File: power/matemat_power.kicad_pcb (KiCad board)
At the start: 2 copper layers, 220 x 77 mm, 153 parts, among them IC1 74HC4094, IC2 74HC4094, IC3 ULN2803A, IC4 PC817, J1 B3_Wago, J101 Output, J11 CONN_8, J2 B3_Wago, J201 Output, J3 B3_Wago, J301 Output, J4 MAIN_BOARD_BUS, J401 Output, J501 Output, J6 B3_Wago, J601 Output, J7 B3_Wago, J701 Output, J801 Output, Q1 NPN_BCE, Q4 ZXMP7A17G, T101 BT136, T201 BT136, T301 BT136, T401 BT136, T501 BT136, T601 BT136, T701 BT136, T801 BT136, U101 MOC3022M, U201 MOC3022M, U301 MOC3022M, U401 MOC3022M, U501 MOC3022M, U6 TPS40200D, U601 MOC3022M, U701 MOC3022M, U801 MOC3022M

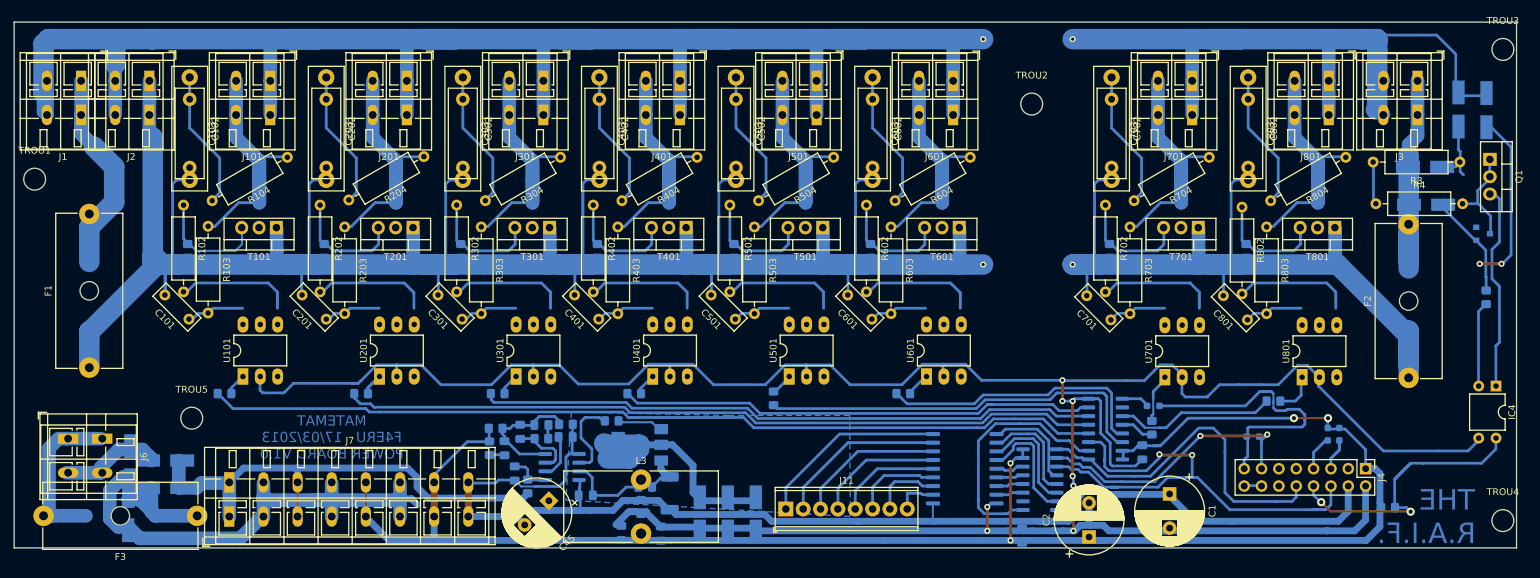
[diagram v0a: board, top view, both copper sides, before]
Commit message: Replaced power board diode pad layouts
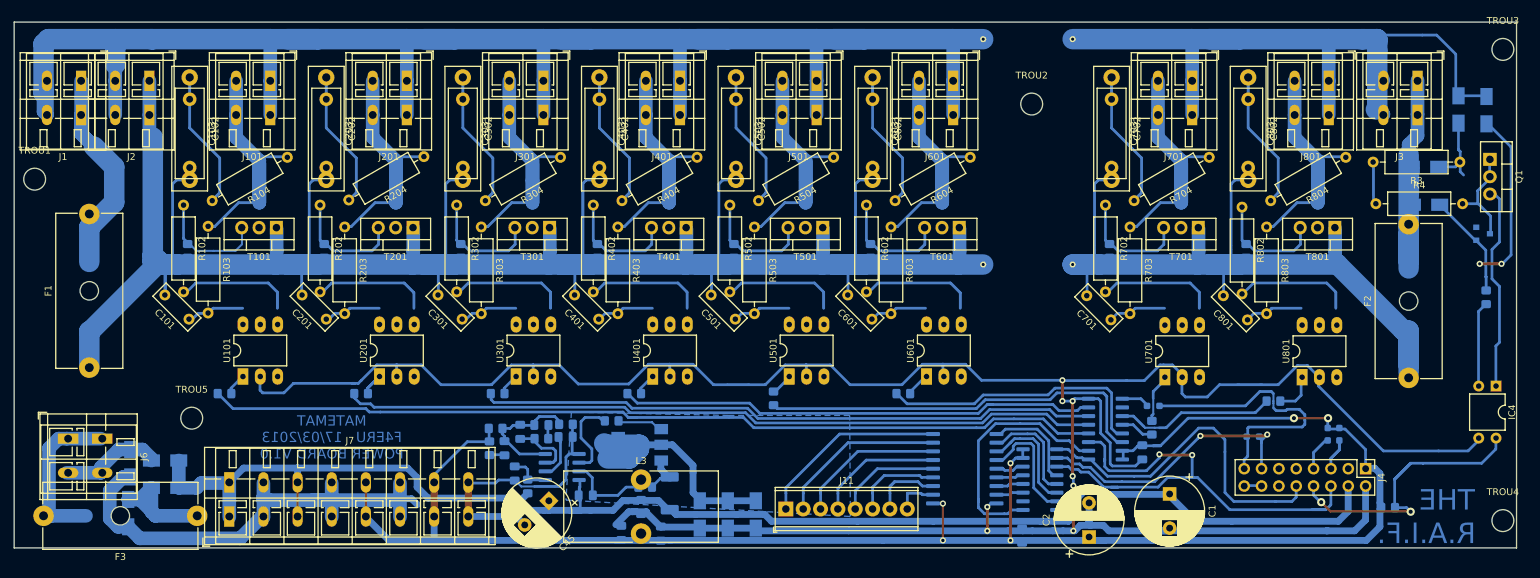
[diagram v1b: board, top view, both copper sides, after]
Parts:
- D1, D10, D11, D2, D3, D4, D5, D6, D7, D8, D9: footprint Diode_SMD:D_SMA_Handsoldering -> Diode_SMD:D_SMA
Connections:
- net Net-(D5-Pad1) renamed /logic_psu/PFET_DRAIN
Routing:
- net +12V: track 273.5 -> 280.3 mm, vias 4 -> 6
- net +28V: track 220.6 -> 217.6 mm
- added copper zone on B.Cu, net /logic_psu/PFET_DRAIN
- removed copper zone on B.Cu, net N-000066
